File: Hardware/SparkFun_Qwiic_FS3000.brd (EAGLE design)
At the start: 25.4 x 25.4 mm, 51 parts, among them J2 QWIIC_RA, U1 FS3000

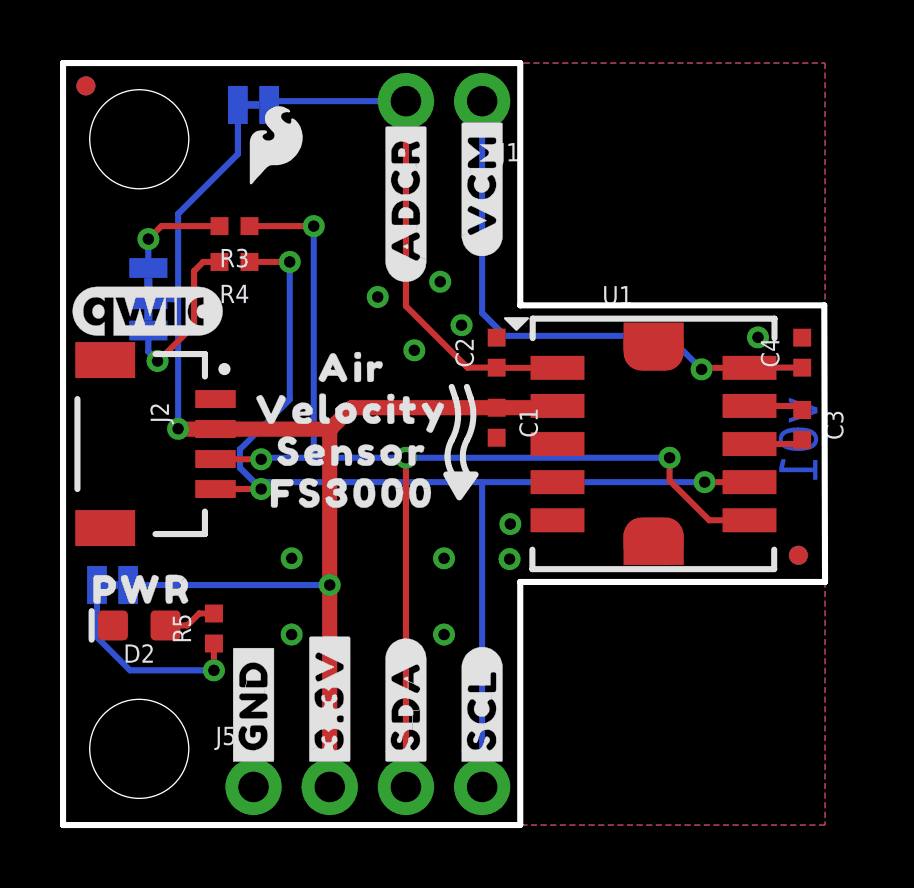
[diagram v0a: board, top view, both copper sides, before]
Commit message: Group Review Changes
-Buzzard labels on VCM/ADCR changed to be correct inputs/outputs end type
-Added in solder pads for two versions (7.23m/s vs 15m/s) (1005/1015)
-Moved"supply range" to below the IC and change to "VDD range".
-schematic cleanup - power LED jumper paragraph. space in I2C address.
-added space between "I2C address" and "0x28" in board silk
-added name/flame logo to board silk.
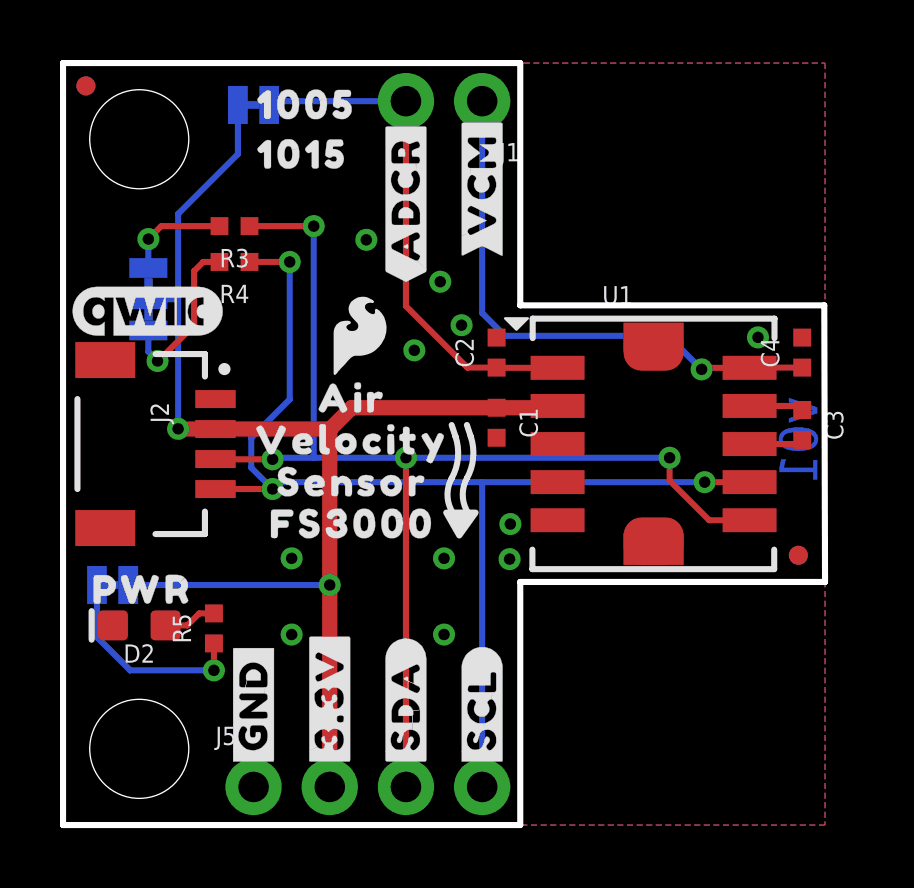
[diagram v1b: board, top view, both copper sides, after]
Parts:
- removed LOGO2: SFE_LOGO_FLAME.1_INCH, SparkFun-Aesthetics:SFE_LOGO_FLAME_.1
- removed U$12: (no value), output:I2C_ADD#0X280
- added LOGO5: SFE_LOGO_NAME_FLAME.1_INCH, SparkFun-Aesthetics:SFE_LOGO_NAME_FLAME_.1
- added U$23: (no value), output:10050
- added U$26: (no value), output:10150
- added U$28: (no value), output:I2C_ADR#_0X280
- moved LOGO3 6.94 mm to (9.88, 16.3)
- moved LOGO1 6.55 mm to (23.5, 13.0)
- moved U$17 4.07 mm to (6.35, 12.3)
- moved U$20 4.07 mm to (9.14, 12.3)
- moved U$21 4.07 mm to (10.5, 12.6)
- moved U$22 4.07 mm to (7.75, 12.3)
- moved U$14 1.02 mm to (9.65, 10.0)
- moved U$16 1.02 mm to (9.65, 12.8)
- moved U$18 1.02 mm to (9.65, 14.2)
- moved U$19 1.02 mm to (9.65, 11.4)
- moved U$15 0.38 mm to (6.35, 23.6)
